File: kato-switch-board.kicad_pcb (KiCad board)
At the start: 4 copper layers, 100 x 100 mm, 151 parts, among them J1 Conn_01x08, J10 Conn_02x05_Odd_Even, J11 Conn_02x05_Odd_Even, J12 Conn_02x05_Odd_Even, J13 Conn_02x05_Odd_Even, J14 Conn_02x05_Odd_Even, J15 Conn_02x05_Odd_Even, J16 Conn_02x05_Odd_Even, J17 Conn_02x05_Odd_Even, J18 Conn_02x05_Odd_Even, J19 Conn_02x05_Odd_Even, J2 Conn_01x08, J20 Conn_02x05_Odd_Even, J21 Conn_02x05_Odd_Even, J22 Conn_02x05_Odd_Even, J23 Conn_02x05_Odd_Even, J24 Conn_02x05_Odd_Even, J25 Conn_02x05_Odd_Even, J26 Conn_02x05_Odd_Even, J27 Conn_02x05_Odd_Even, J28 Conn_01x02, J29 Conn_01x02, J3 Conn_01x08, J30 Conn_01x02, J31 Conn_01x02, J32 Conn_01x02, J33 Conn_01x02, J34 Conn_01x02, J35 Conn_01x02, J36 Conn_01x02, J37 Conn_01x02, J38 Conn_01x02, J39 Conn_01x02, J4 Conn_01x08, J40 Conn_01x02, J5 Conn_01x02, J6 Barrel_Jack_MountingPin, J7 Conn_02x02_Odd_Even, J8 Conn_02x02_Odd_Even, J9 Conn_02x02_Odd_Even, U1 74HC238, U10 TLC59282DBQR...SM16206, U11 TLC59282DBQR...SM16206, U12 PCA9617ADPJ, U13 PT5126A, U14 PT5126A, U15 PT5126A, U16 PT5126A, U17 PT5126A, U18 PT5126A, U19 PT5126A, U2 74HC238, U20 PT5126A, U21 PT5126A, U22 PT5126A, U23 PT5126A, U24 PT5126A, U25 6N137, U3 74HC238, U4 TLC59282DBQR...SM16206, U5 TLC59282DBQR...SM16206, U6 TLC59282DBQR...SM16206, U7 TLC59282DBQR...SM16206, U8 TLC59282DBQR...SM16206, U9 TLC59282DBQR...SM16206

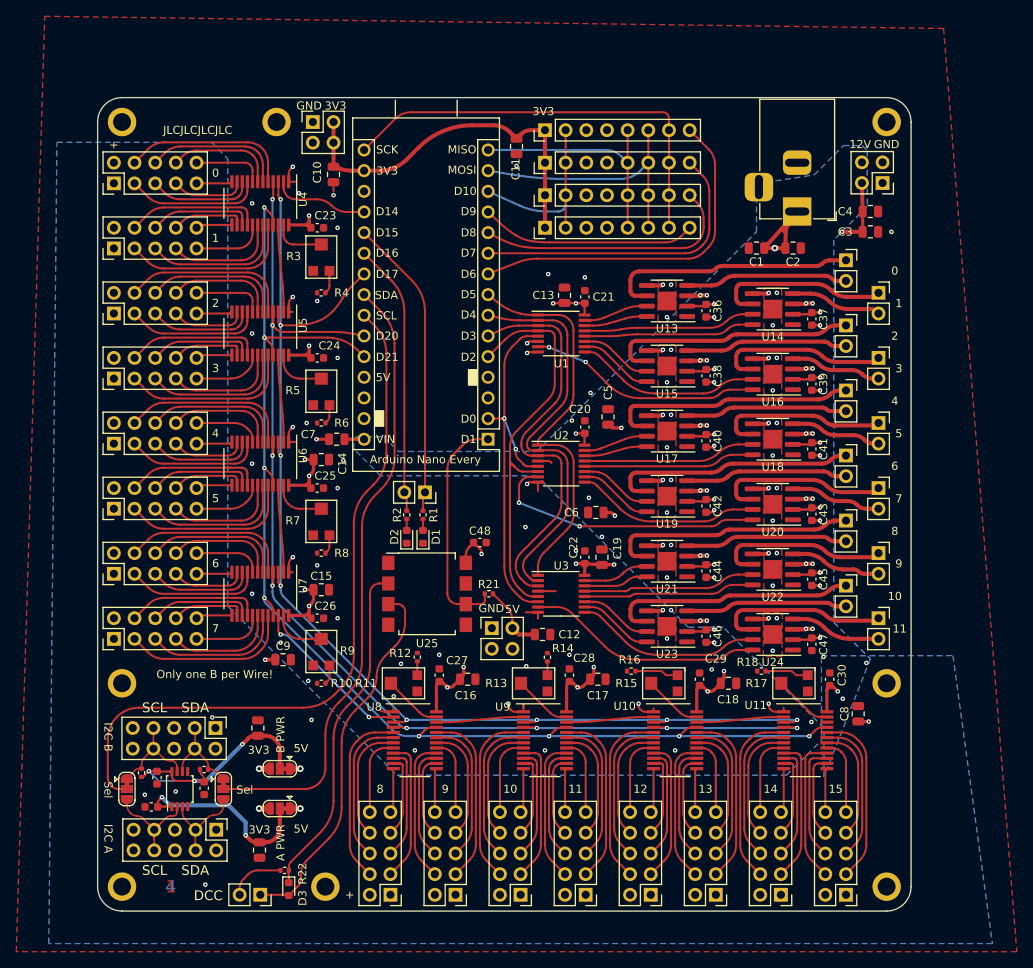
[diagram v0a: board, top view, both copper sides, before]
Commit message: silkscreen & pad changes
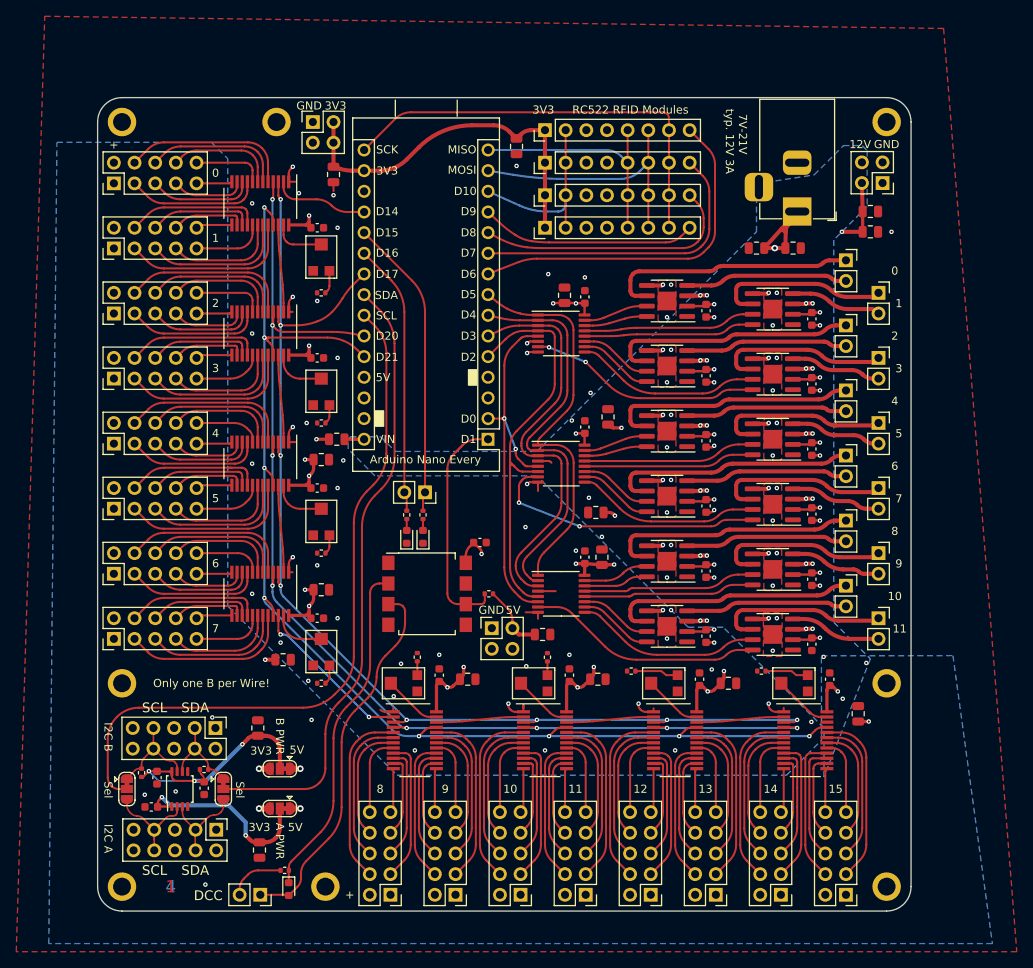
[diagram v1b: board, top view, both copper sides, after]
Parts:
- added REF**: KiCad-Logo2_12mm_SilkScreen, Symbol:KiCad-Logo2_12mm_SilkScreen, B.Cu at (122.7, 65.0)
- JP3, JP4: value SolderJumper_3_Bridged12 -> Jumper
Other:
- board text added: "7V-21V typ. 12V 3A"
- board text added: "RC522 RFID Modules"
- board text added: "github.com/precap/kato-switch-board"

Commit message: use only rounded pads
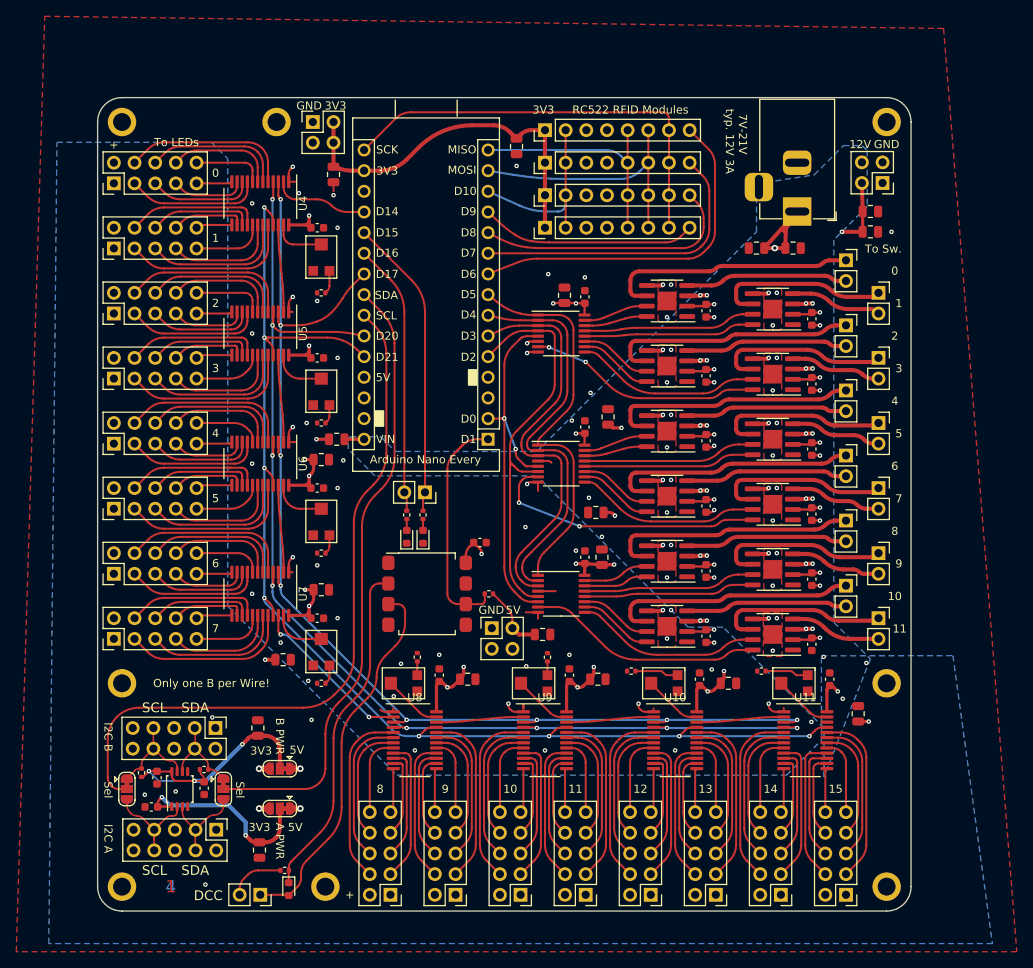
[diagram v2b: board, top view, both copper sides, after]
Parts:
- U10, U11, U4, U5, U6, U7, U8, U9: footprint Package_SO:QSOP-24_3.9x8.7mm_P0.635mm -> _my:QSOP-24_3.9x8.7mm_P0.635mm_rounded_pads
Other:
- board text added: "To LEDs"
- board text added: "To Sw."
